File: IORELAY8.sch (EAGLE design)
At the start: 54 parts, among them Q1 2N7002, Q2 2N7002, Q3 2N7002, Q4 2N7002, Q5 2N7002, Q6 2N7002, Q7 2N7002, Q8 2N7002

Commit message: Resized board on metric grid
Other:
- note added: "SKU: IORELAY8"
- note added: "VCC is VIN from host"
- note added: "www.superhouse.tv/iorelay8"
- note removed: "SKU: IOR8"
- note removed: "www.superhouse.tv/ior8"
- moved on the sheet: D1, D2, D3, D4, D5, D6, D7, D8, JP1, JP2, JP3, JP4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

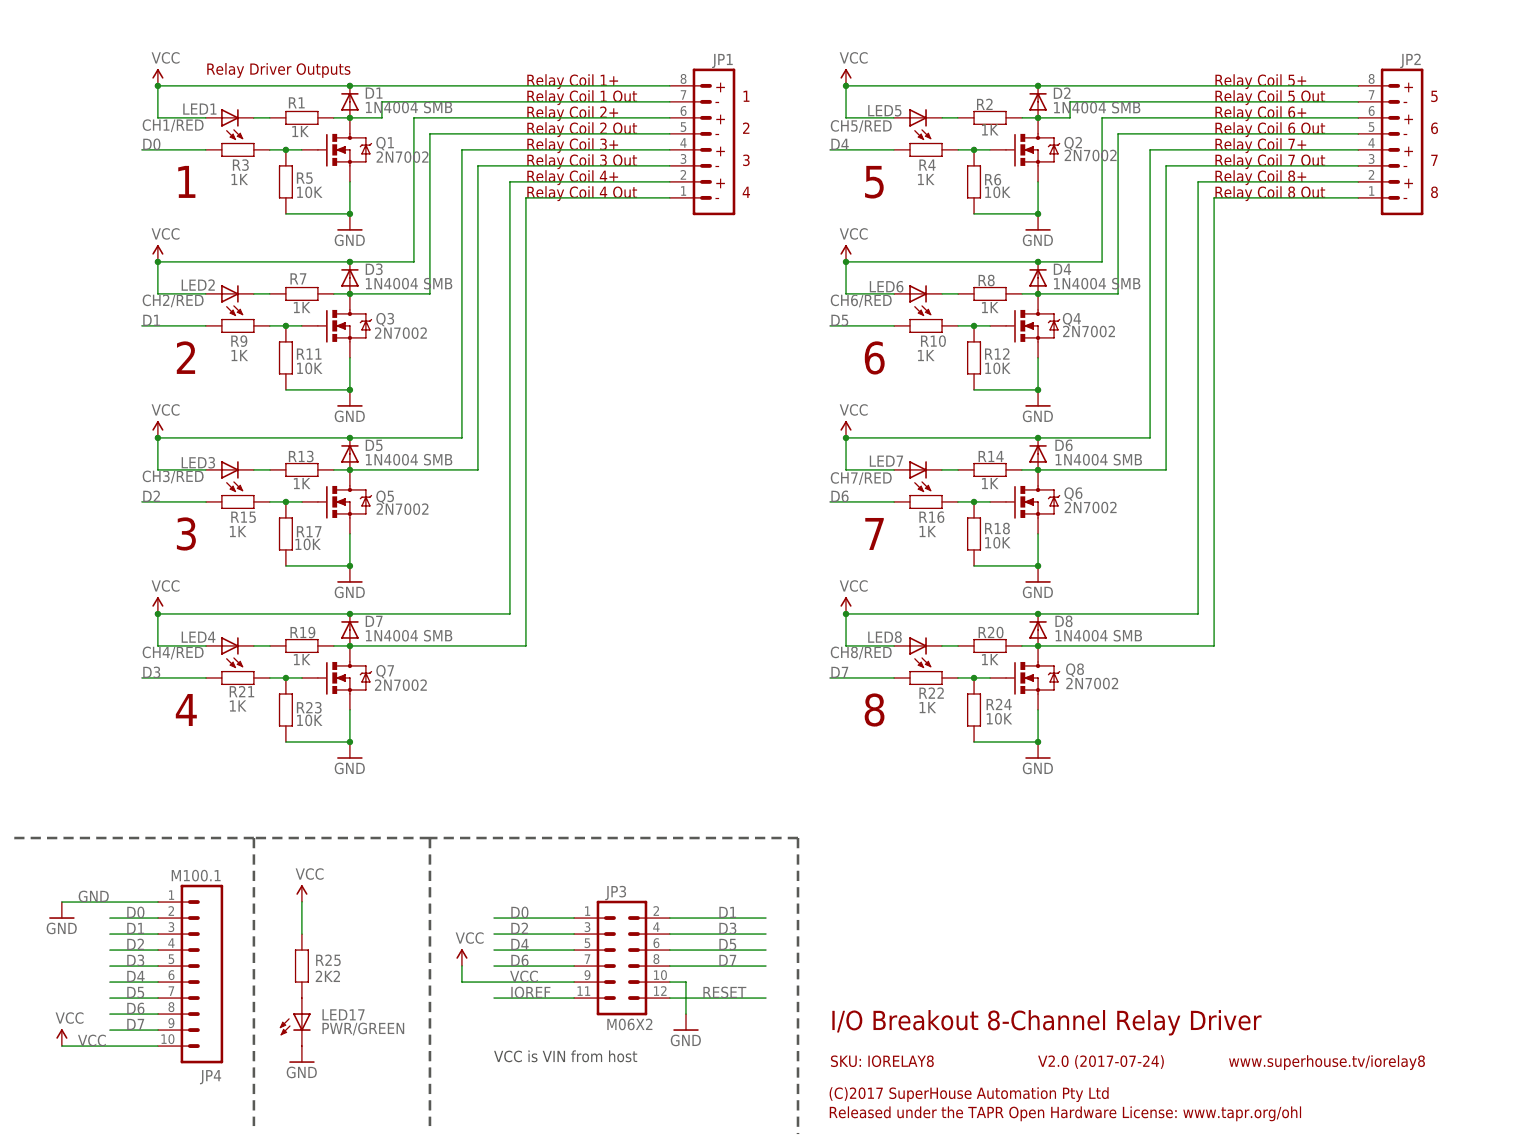
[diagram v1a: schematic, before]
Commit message: Replaced most parts using SuperHouse library to add 3D models
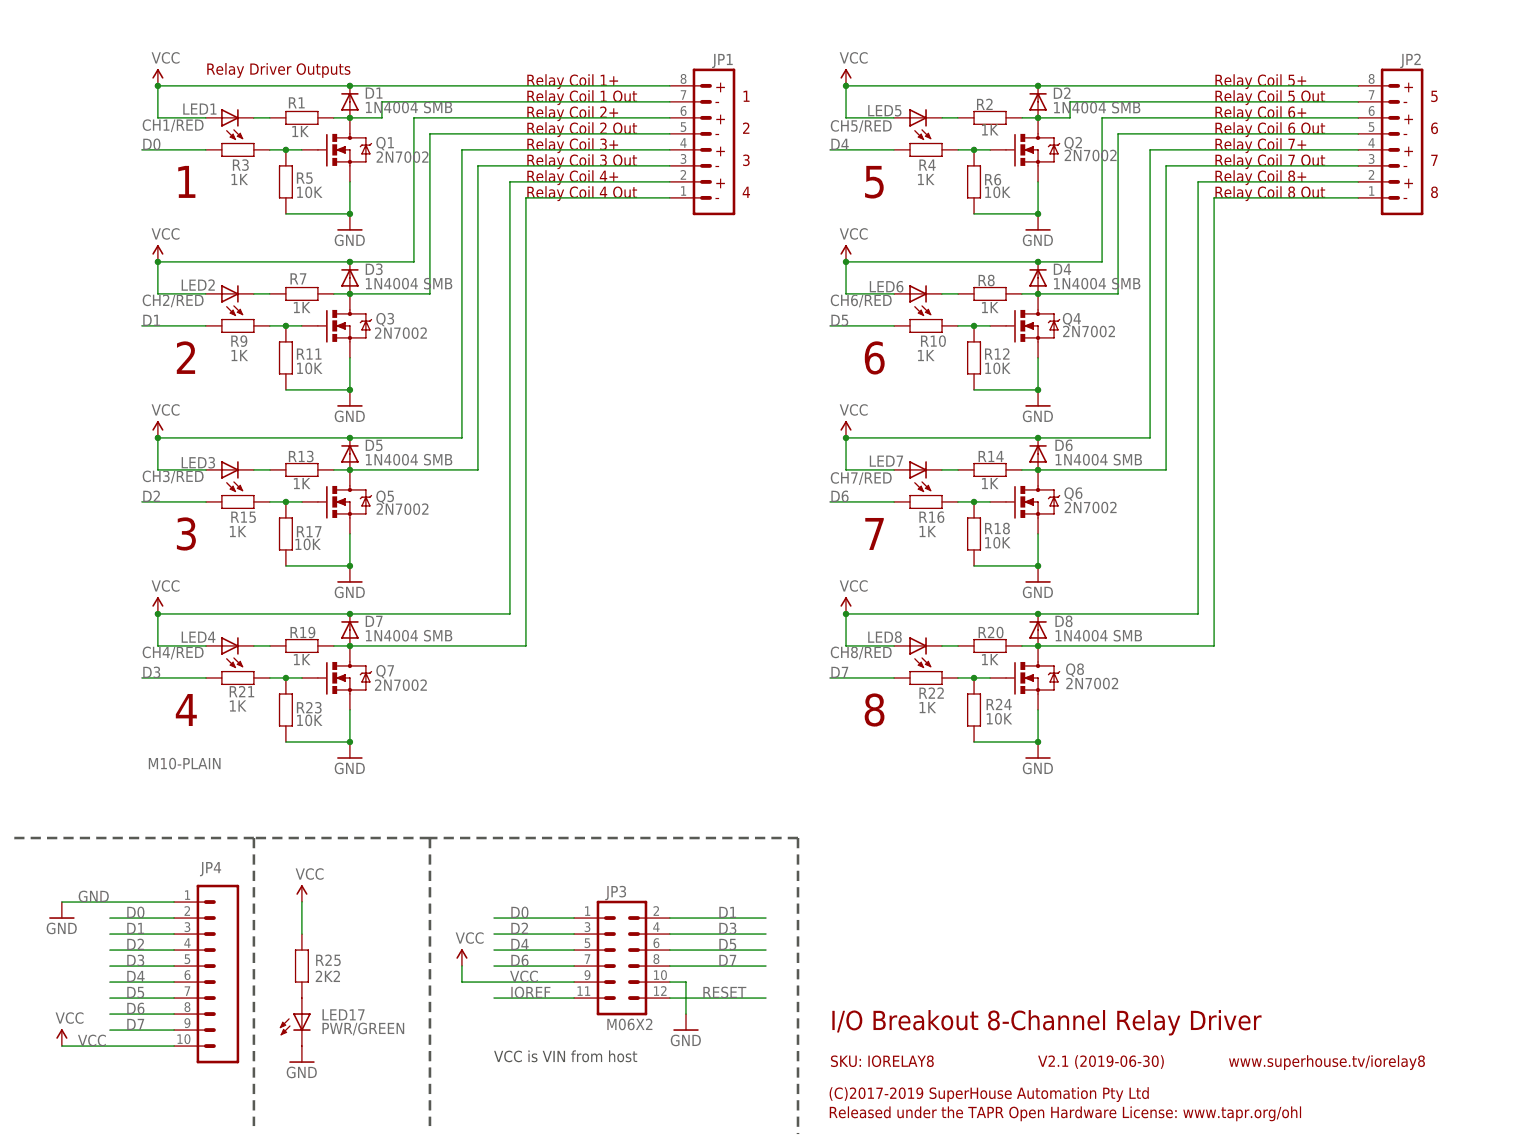
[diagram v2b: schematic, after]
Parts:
- D1, D2, D3, D4, D5, D6, D7, D8: device freetronics-master-v1.1:DIODESMB -> SuperHouse-DiscreteSemi:DIODESMA
- JP4: value M100.1 -> M10-PLAIN; device freetronics-original:M100.1 -> SuperHouse-Connectors:M10-PLAIN
- LED1, LED17, LED2, LED3, LED4, LED5, LED6, LED7, LED8: device freetronics-master-v1:LED0603 -> SuperHouse-LEDs:LED0603
- Q1, Q2, Q3, Q4, Q5, Q6, Q7, Q8: device freetronics-master-v1:MOSFET-NCHANNELSMD -> SuperHouse-DiscreteSemi:MOSFET-NCHANNEL-233
- R1, R10, R11, R12, R13, R14, R15, R16, R17, R18, R19, R2, R20, R21, R22, R23, R24, R25, R3, R4, R5, R6, R7, R8, R9: device freetronics-master-v1:RESISTOR0603 -> SuperHouse-DiscreteSemi:RESISTOR0603
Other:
- note added: "(C)2017-2019 SuperHouse Automation Pty Ltd"
- note added: "V2.1 (2019-06-30)"
- note removed: "(C)2017 SuperHouse Automation Pty Ltd"
- note removed: "V2.0 (2017-07-24)"
- moved on the sheet: JP4

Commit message: Replaced parts using SuperHouse libraries to add 3D models
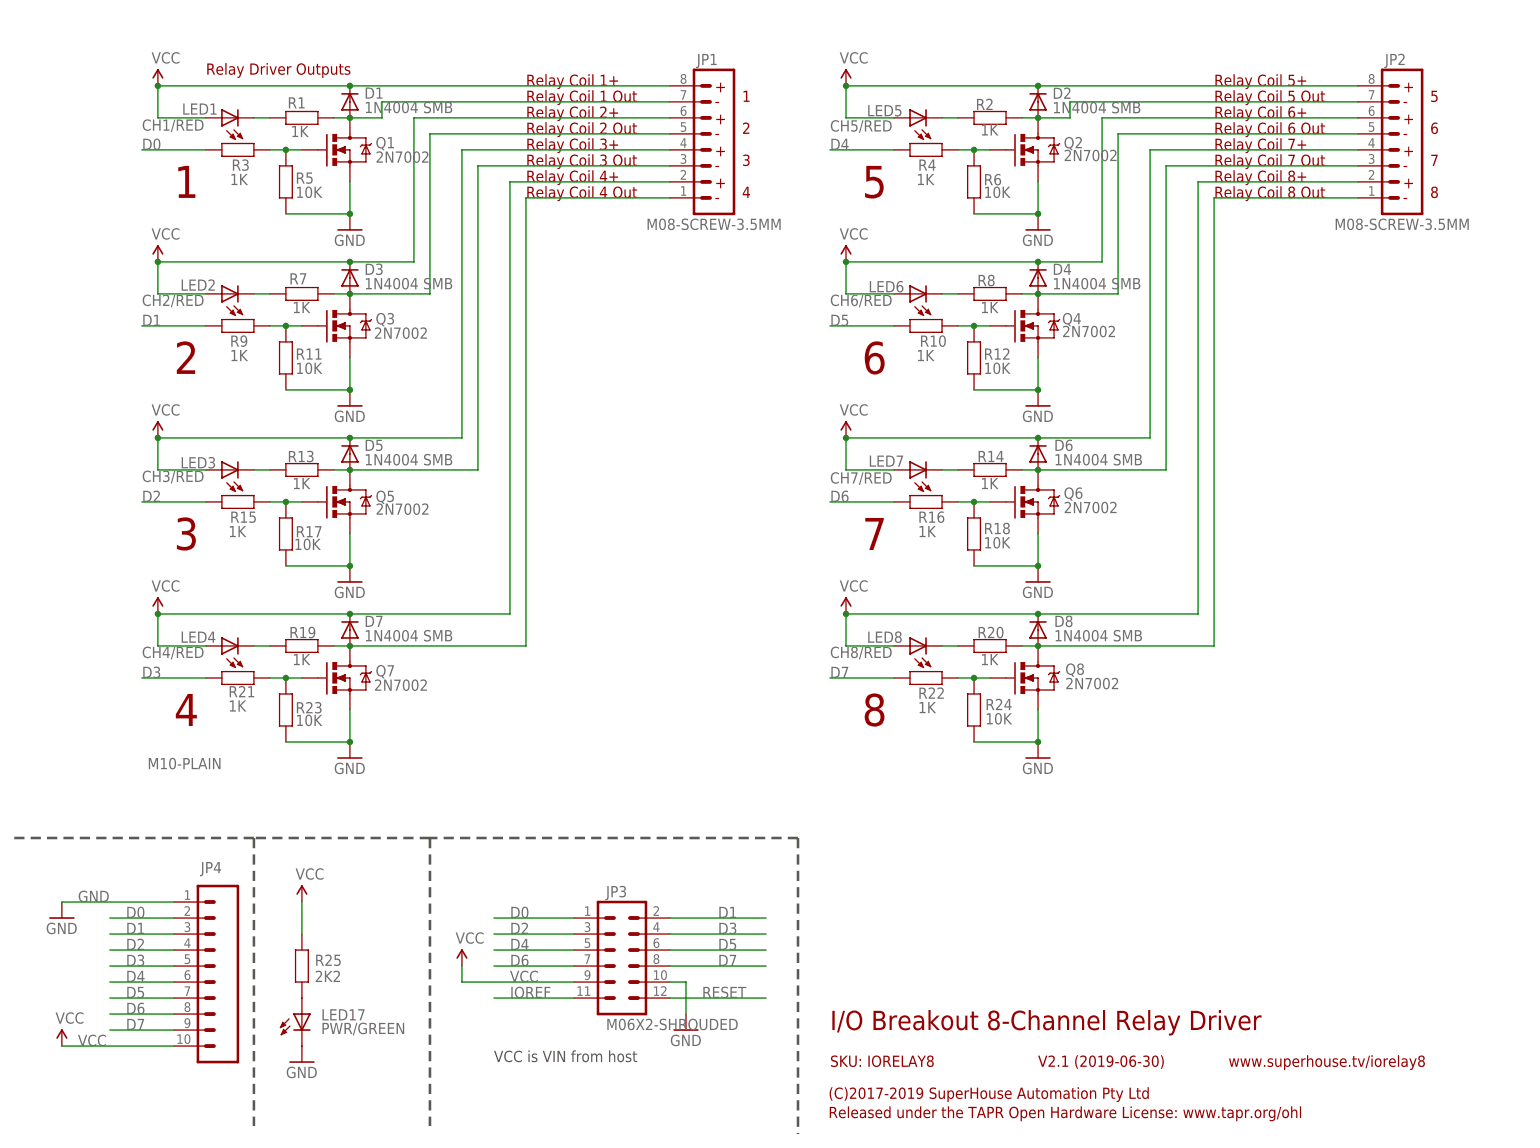
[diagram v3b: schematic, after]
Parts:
- JP1, JP2: value (none) -> M08-SCREW-3.5MM; device freetronics-master-v1:M08 -> SuperHouse-Connectors:M08-SCREW-3.5MM
- JP3: value M06X2 -> M06X2-SHROUDED; device freetronics-jon:M06X2 -> SuperHouse-Connectors:M06X2-SHROUDED
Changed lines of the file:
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@@
 <part name="GND24" library="freetronics" deviceset="GND" device=""/>
 <part name="R25" library="SuperHouse-DiscreteSemi" library_urn="urn:adsk.eagle:library:11768461" deviceset="RESISTOR" device="0603" package3d_urn="urn:adsk.eagle:package:11768543/2" value="2K2"/>
-<part name="JP1" library="freetronics-master-v1" deviceset="M08" device=""/>
-<part name="JP2" library="freetronics-master-v1" deviceset="M08" device=""/>
-<part name="JP3" library="freetronics-jon" deviceset="M06X2" device=""/>
+<part name="JP1" library="SuperHouse-Connectors" library_urn="urn:adsk.eagle:library:11765989" deviceset="M08" device="-SCREW-3.5MM" package3d_urn="urn:adsk.eagle:package:12194855/2"/>
+<part name="JP2" library="SuperHouse-Connectors" library_urn="urn:adsk.eagle:library:11765989" deviceset="M08" device="-SCREW-3.5MM" package3d_urn="urn:adsk.eagle:package:12194855/2"/>
+<part name="JP3" library="SuperHouse-Connectors" library_urn="urn:adsk.eagle:library:11765989" deviceset="M06X2" device="-SHROUDED" package3d_urn="urn:adsk.eagle:package:11976015/2"/>
 <part name="GND2" library="freetronics" deviceset="GND" device=""/>
 <part name="P+1" library="freetronics-original" deviceset="VCC" device=""/>
@@
 <attribute name="VALUE" x="52.832" y="29.718" size="1.778" layer="96" rot="MR180"/>
 </instance>
-<instance part="JP1" gate="G$1" x="114.3" y="160.02" smashed="yes" rot="MR0">
-<attribute name="VALUE" x="119.38" y="147.32" size="1.778" layer="96" rot="MR0"/>
-<attribute name="NAME" x="119.38" y="173.482" size="1.778" layer="95" rot="MR0"/>
-</instance>
-<instance part="JP2" gate="G$1" x="223.52" y="160.02" smashed="yes" rot="MR0">
-<attribute name="VALUE" x="228.6" y="147.32" size="1.778" layer="96" rot="MR0"/>
-<attribute name="NAME" x="228.6" y="173.482" size="1.778" layer="95" rot="MR0"/>
+<instance part="JP1" gate="G$1" x="116.84" y="152.4" smashed="yes" rot="MR0">
+<attribute name="VALUE" x="127" y="147.32" size="1.778" layer="96" rot="MR0"/>
+<attribute name="NAME" x="116.84" y="173.482" size="1.778" layer="95" rot="MR0"/>
+</instance>
+<instance part="JP2" gate="G$1" x="226.06" y="152.4" smashed="yes" rot="MR0">
+<attribute name="VALUE" x="236.22" y="147.32" size="1.778" layer="96" rot="MR0"/>
+<attribute name="NAME" x="226.06" y="173.482" size="1.778" layer="95" rot="MR0"/>
 </instance>
 <instance part="JP3" gate="G$1" x="101.6" y="33.02" smashed="yes">

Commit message: Silkscreen change for v2.2 release
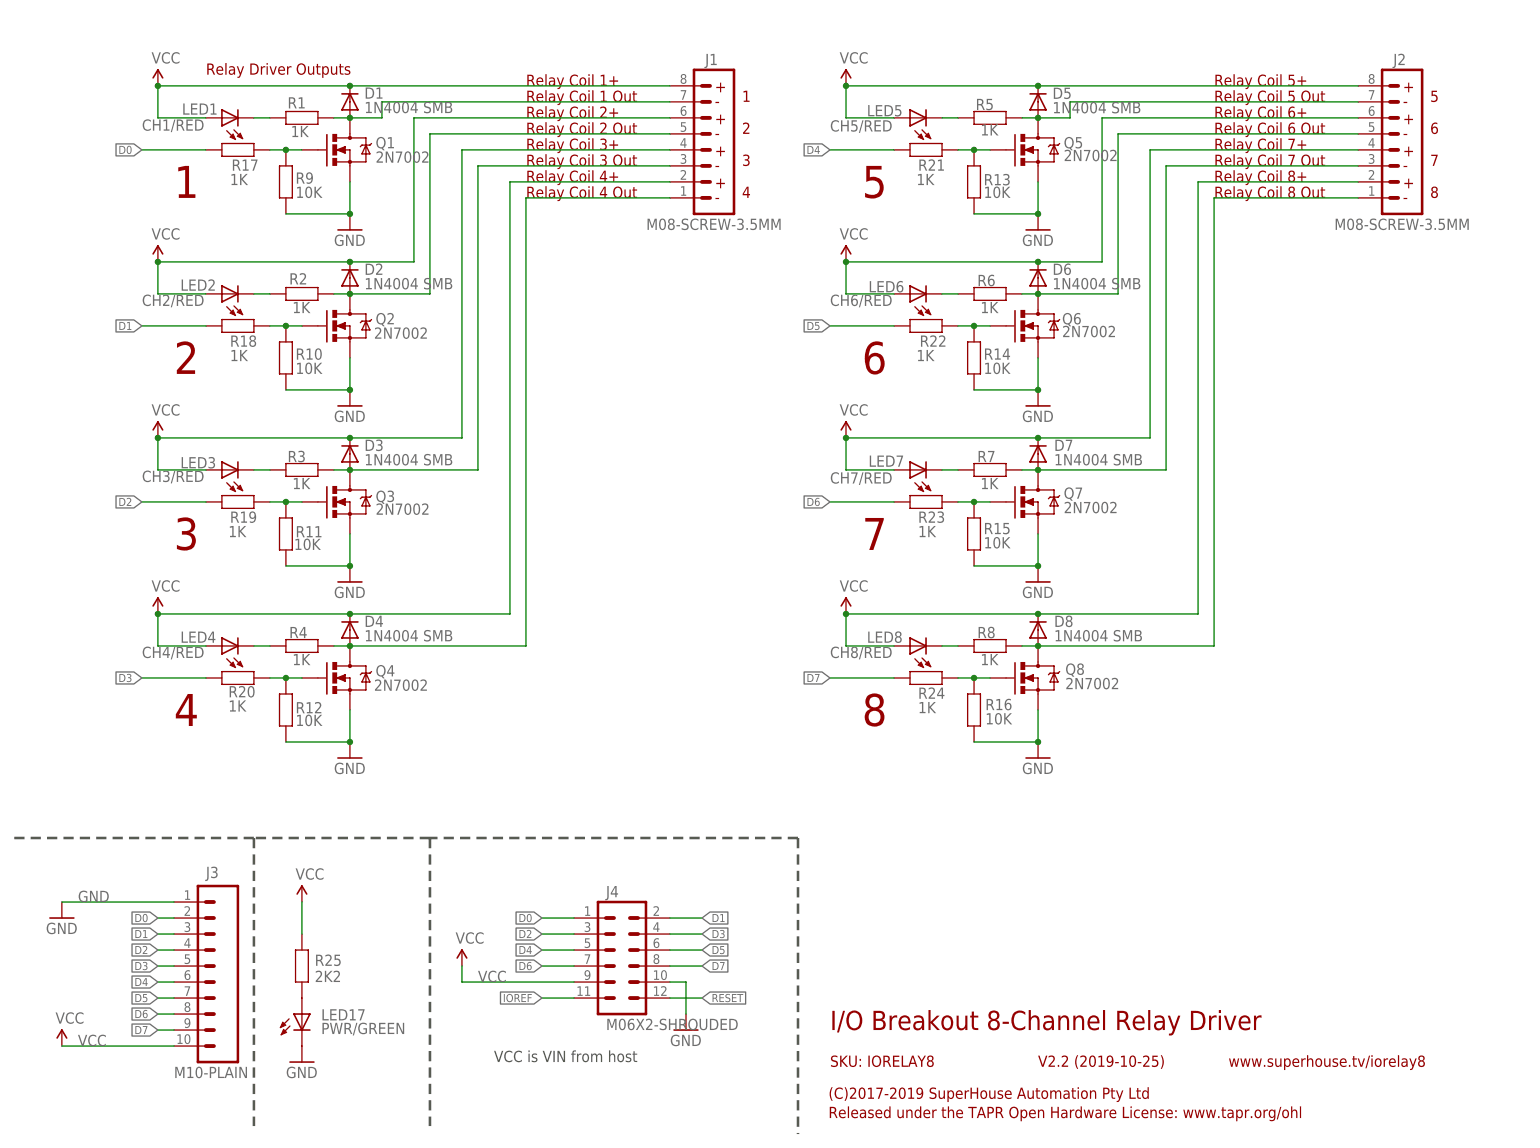
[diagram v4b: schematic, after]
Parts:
- R10, R13, R14, R15, R16, R9: value 1K -> 10K
- R17, R18, R23, R24, R5, R6: value 10K -> 1K
- renumbered JP1 to J1, JP2 to J2, JP3 to J4, JP4 to J3
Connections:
- net D0: now also R17.2; no longer R3.2
- net D1: now also R18.2; no longer R9.2
- net D2: now also R19.2; no longer R15.2
- net D3: now also R20.2; no longer R21.2
- net D4: now also R21.2; no longer R4.2
- net D5: now also R22.2; no longer R10.2
- net D6: now also R23.2; no longer R16.2
- net D7: now also R24.2; no longer R22.2
- net GND: now also R10.1, R13.1, R14.1, R15.1, R16.1, R9.1; no longer R17.1, R18.1, R23.1, R24.1, R5.1, R6.1
- net N$1: now also R17.1, R9.2; no longer R3.1, R5.2
- net N$10: now also Q3.G, R11.2, R19.1; no longer Q5.G, R15.1, R17.2
- net N$11: now also D4.A, Q4.D, R4.2; no longer D7.A, Q7.D, R19.2
- net N$12: now also Q4.G, R12.2, R20.1; no longer Q7.G, R21.1, R23.2
- net N$13: now also D5.A, Q5.D, R5.2; no longer D2.A, Q2.D, R2.2
- net N$14: now also Q5.G, R13.2, R21.1; no longer Q2.G, R4.1, R6.2
- net N$15: now also D6.A, Q6.D, R6.2; no longer D4.A, Q4.D, R8.2
- net N$16: now also Q6.G, R14.2, R22.1; no longer Q4.G, R10.1, R12.2
- net N$17: now also D7.A, Q7.D, R7.2; no longer D6.A, Q6.D, R14.2
- net N$18: now also Q7.G, R15.2, R23.1; no longer Q6.G, R16.1, R18.2
- net N$19: now also R8.2; no longer R20.2
- net N$20: now also R16.2, R24.1; no longer R22.1, R24.2
- net N$21: now also R2.1; no longer R7.1
- net N$22: now also R4.1; no longer R19.1
- net N$23: now also R3.1; no longer R13.1
- net N$25: now also R5.1; no longer R2.1
- net N$26: now also R6.1; no longer R8.1
- net N$27: now also R7.1; no longer R14.1
- net N$28: now also R8.1; no longer R20.1
- net N$3: now also D2.A, Q2.D, R2.2; no longer D3.A, Q3.D, R7.2
- net N$8: now also Q2.G, R10.2, R18.1; no longer Q3.G, R11.2, R9.1
- net N$9: now also D3.A, Q3.D, R3.2; no longer D5.A, Q5.D, R13.2
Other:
- note added: "V2.2 (2019-10-25)"
- note removed: "V2.1 (2019-06-30)"
- moved on the sheet: D2, D3, D4, D5, D6, D7, Q2, Q3, Q4, Q5, Q6, Q7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
